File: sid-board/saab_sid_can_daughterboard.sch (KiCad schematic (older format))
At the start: 15 parts, among them Q1 BSS138, Q2 BSS138, Q3 BSS138, Q4 BSS138, U3 PCA82C250, U4 PCA82C250

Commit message: Added beginnings of CAN daughterboard
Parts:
- gave numbers to parts that had none: 1
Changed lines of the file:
@@
 SIMPLE CAN INTERFACE WITH\nLOGIC LEVEL SHIFTING.\nINTENTED TO INTERFACE WITH ESP32 MICROCONTROLLER OR SIMILAR.
 $Comp
-L Connector_Generic:Conn_02x10_Counter_Clockwise J?
+L Connector_Generic:Conn_02x10_Counter_Clockwise J1
 U 1 1 5E564141
 P 1700 3800
-F 0 "J?" H 1750 4417 50  0000 C CNN
+F 0 "J1" H 1750 4417 50  0000 C CNN
 F 1 "Conn_02x10_Counter_Clockwise" H 1750 4326 50  0000 C CNN
 F 2 "Connector_PinSocket_2.54mm:PinSocket_2x10_P2.54mm_Vertical" H 1700 3800 50  0001 C CNN

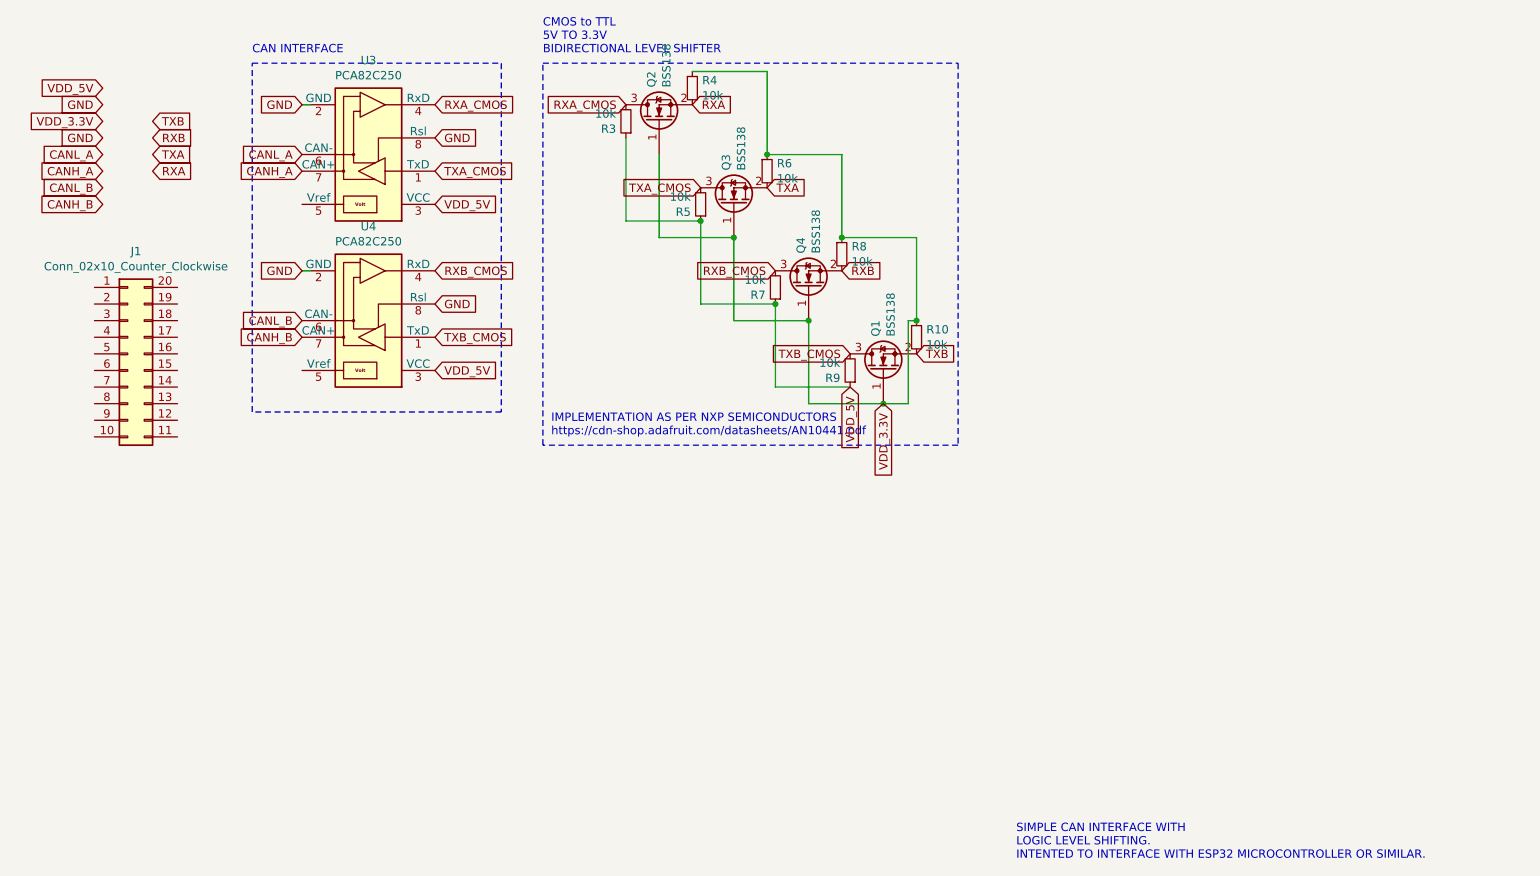
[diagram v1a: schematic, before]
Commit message: Working on CAN daughterboard
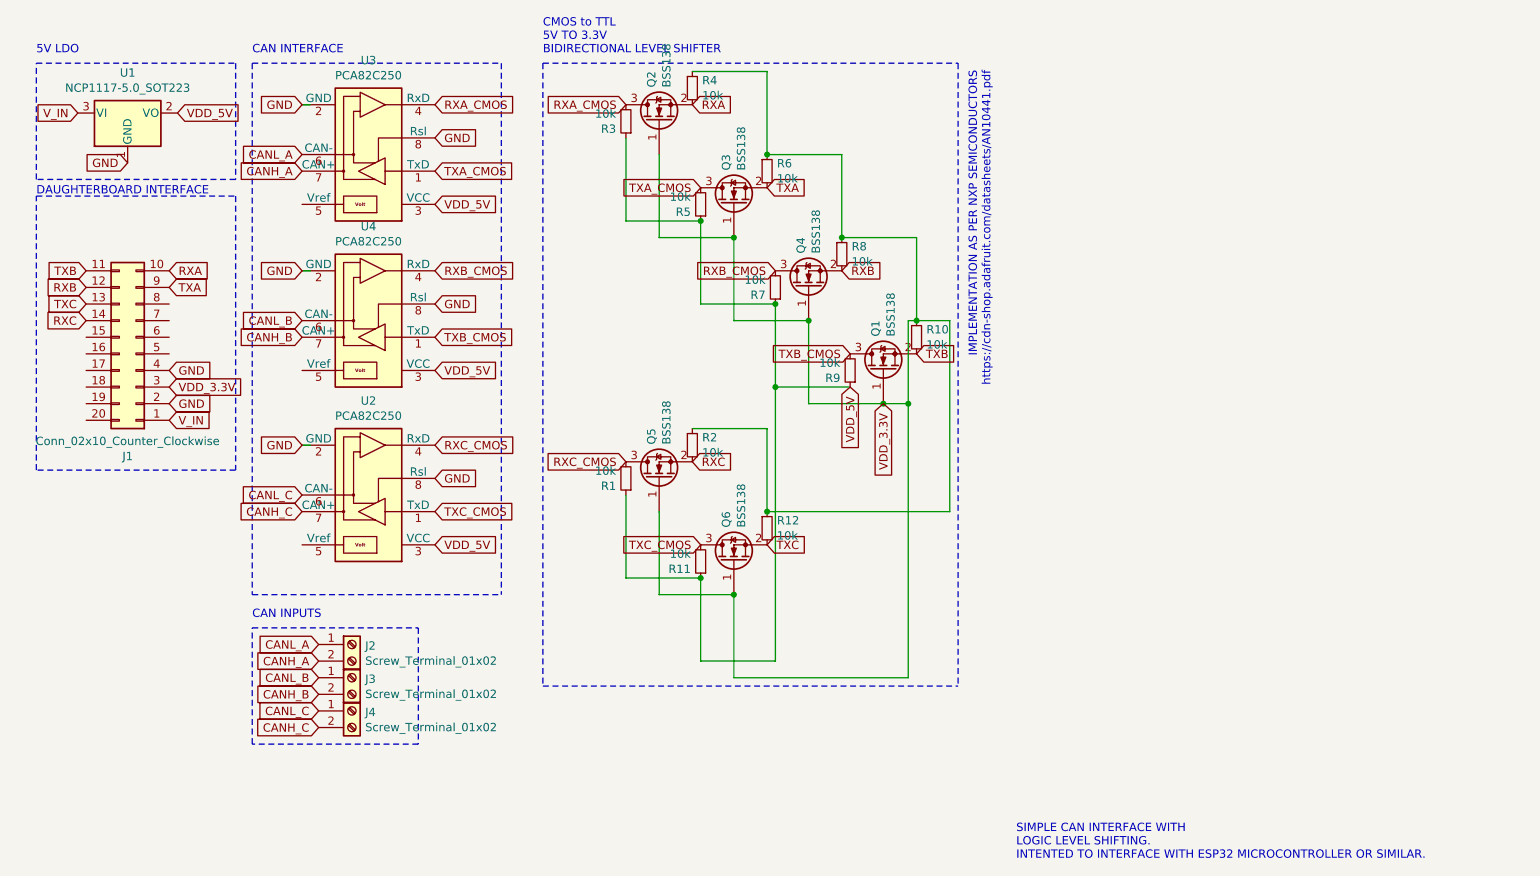
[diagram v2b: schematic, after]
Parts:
- added J2, J3, J4: Screw_Terminal_01x02, TerminalBlock_Phoenix:TerminalBlock_Phoenix_MKDS-1,5-2-5.08_1x02_P5.08mm_Horizontal, symbol Connector:Screw_Terminal_01x02
- added Q5, Q6: BSS138, Package_TO_SOT_SMD:SOT-23, symbol Transistor_FET:BSS138
- added R1, R11, R12, R2: 10k, Resistor_SMD:R_0805_2012Metric_Pad1.15x1.40mm_HandSolder, symbol Device:R_Small
- added U1: NCP1117-5.0_SOT223, Package_TO_SOT_SMD:SOT-223-3_TabPin2, symbol Regulator_Linear:NCP1117-5.0_SOT223
- added U2: PCA82C250, Package_SO:SOIC-8_3.9x4.9mm_P1.27mm, symbol local_symbols:PCA82C250
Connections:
- net labels added: CANH_C, CANL_C, RXC, RXC_CMOS, TXC, TXC_CMOS, V_IN
- wire segments 23 -> 39
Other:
- note added: "5V LDO"
- note added: "CAN INPUTS"
- note added: "DAUGHTERBOARD INTERFACE"
- moved on the sheet: J1
